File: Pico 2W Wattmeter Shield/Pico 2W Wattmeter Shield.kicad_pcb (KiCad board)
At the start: 2 copper layers, 53.3 x 22.9 mm, 23 parts, among them J1 RF In, U1 ADL5904, U2 ADS1115IDGS

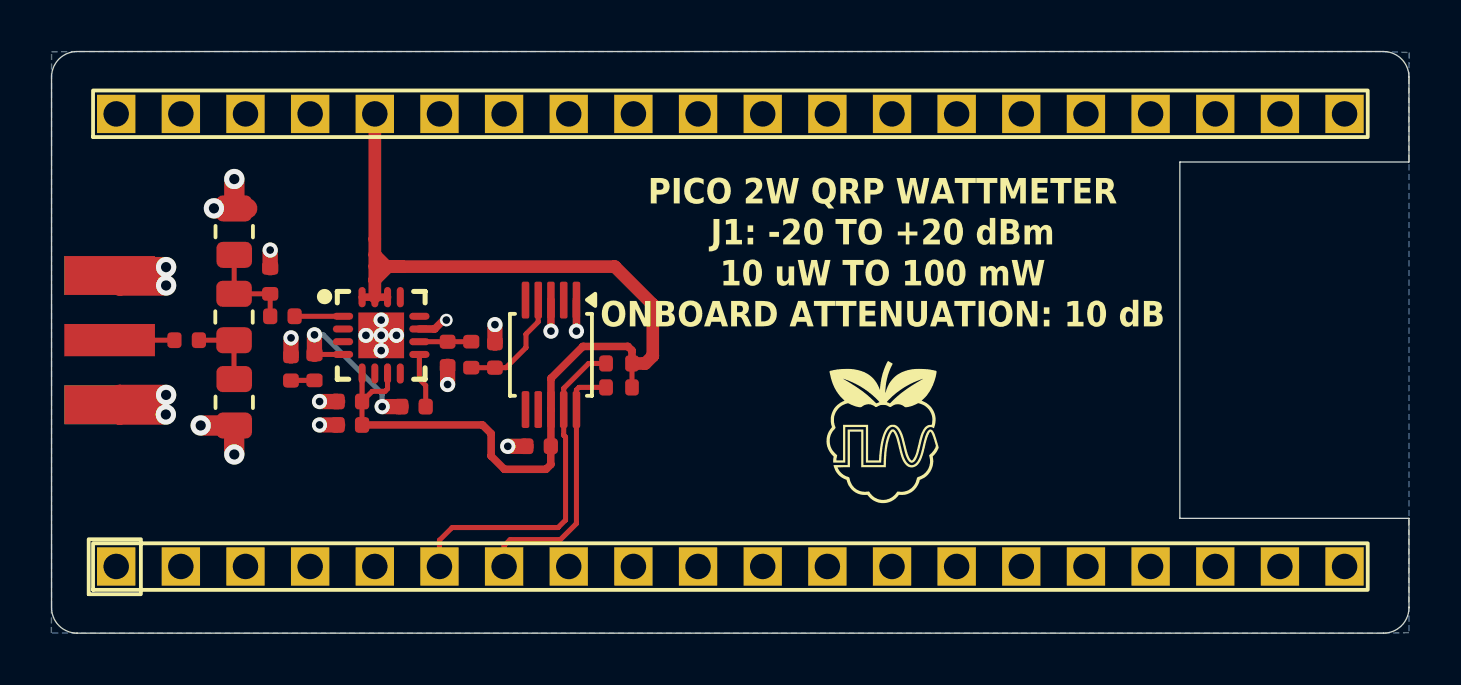
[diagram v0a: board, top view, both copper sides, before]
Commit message: Flip Pico shield assemblies and center USB reference markings
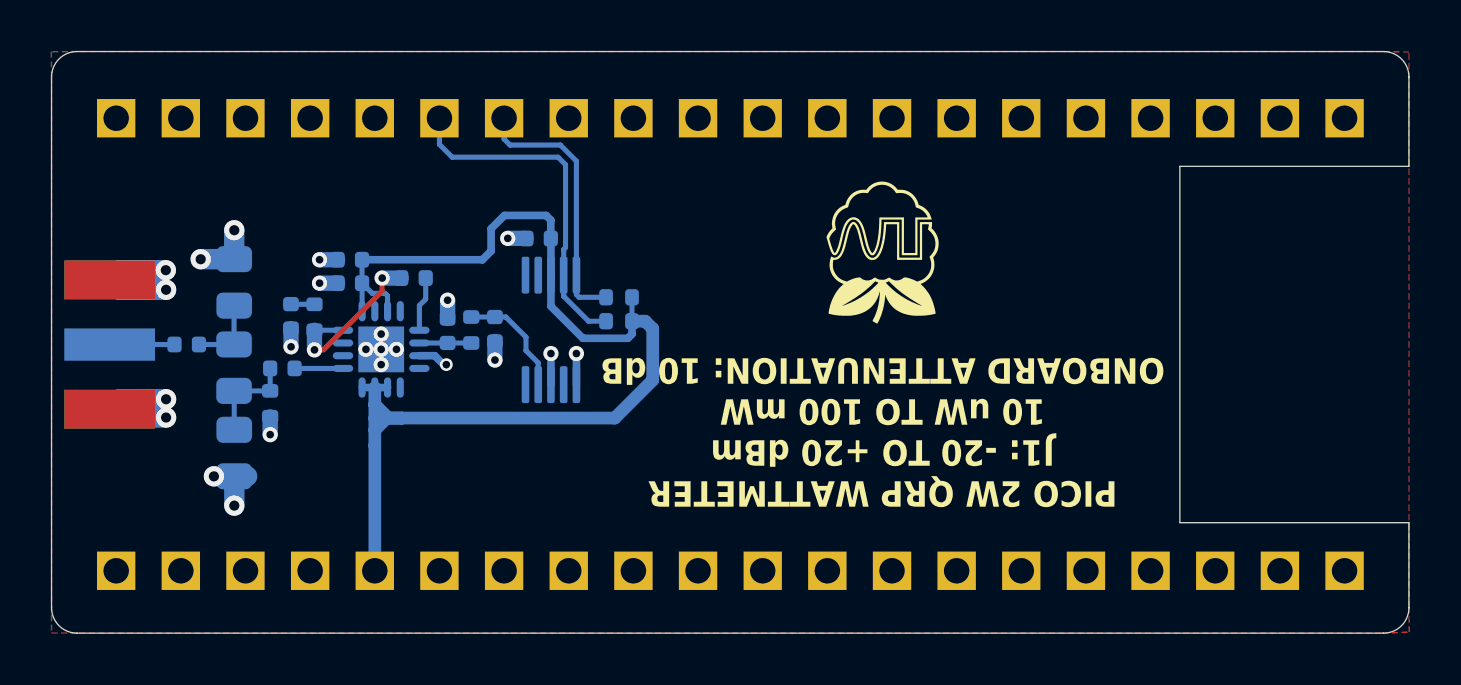
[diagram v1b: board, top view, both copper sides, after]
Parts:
- C1, C2, C3, C4, C5, C6, C7, C8, C9, J1, LOGO1, R1, R2, R3, R4, R5, R6, R7, R8, U1, U2, U3: moved to B.Cu
- LOGO2: moved to F.Cu
- moved R3 8.70 mm to (127.3, 94.1), turned to -90 degrees
- moved C9 8.16 mm to (139.3, 85.7)
- moved LOGO1 7.05 mm to (152.8, 86.2)
- moved LOGO2 7.05 mm to (152.8, 86.2)
- moved C5 6.49 mm to (131.8, 86.5)
- moved C6 5.05 mm to (134.3, 87.2)
- moved R4 4.83 mm to (128.7, 92.2), turned to -90 degrees
- moved R1 4.71 mm to (127.3, 87.4), turned to 90 degrees
- moved C4 4.65 mm to (131.8, 87.5)
- moved R7 3.54 mm to (142.4, 88.0)
- moved C2 2.05 mm to (129.2, 90.8)
- moved C3 2.04 mm to (129.5, 88.8), turned to -90 degrees
- moved R2 1.99 mm to (127.3, 90.8), turned to -90 degrees
- moved R5 1.97 mm to (130.5, 88.8), turned to 90 degrees
- moved U3 1.95 mm to (146.8, 90.8), turned to -90 degrees
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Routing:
- added copper zone on F.Cu, net GND
- removed copper zone on B.Cu, net GND
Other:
- outline, holes or cut-outs redrawn

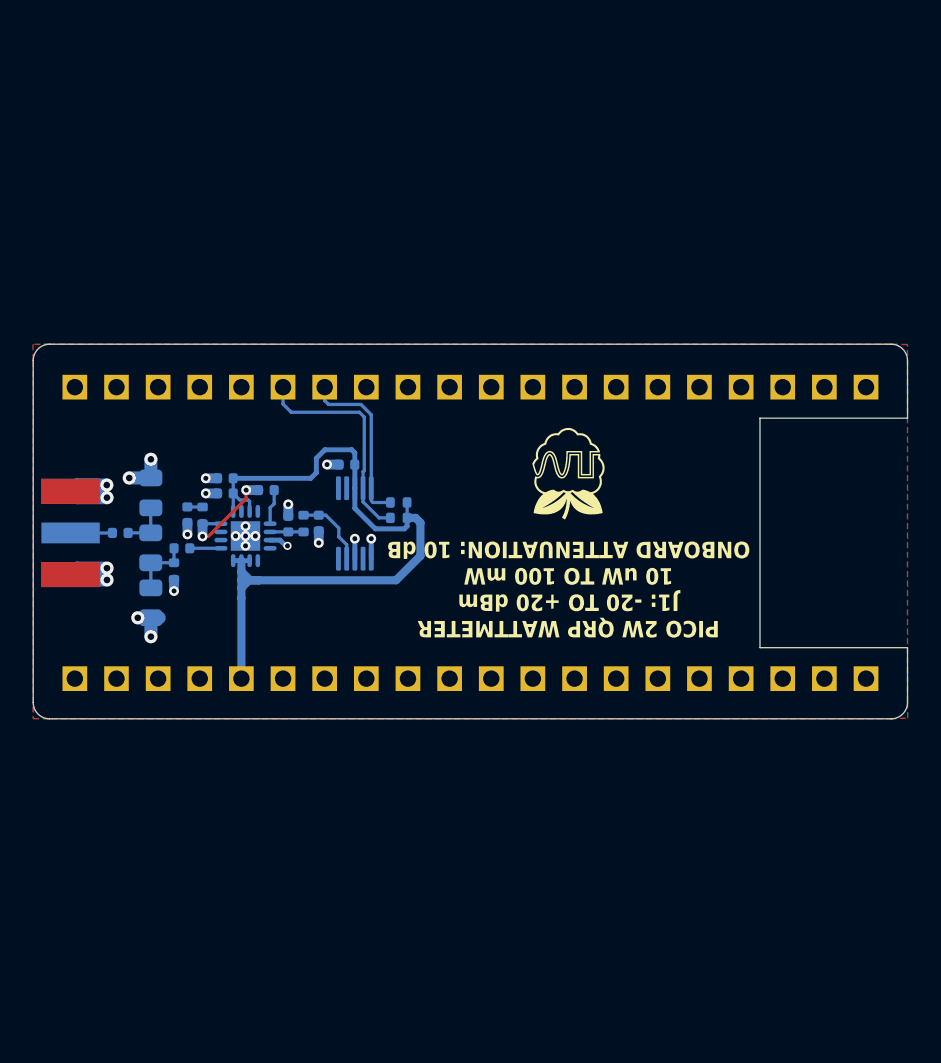
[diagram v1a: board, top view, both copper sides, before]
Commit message: Updated wattmeter design
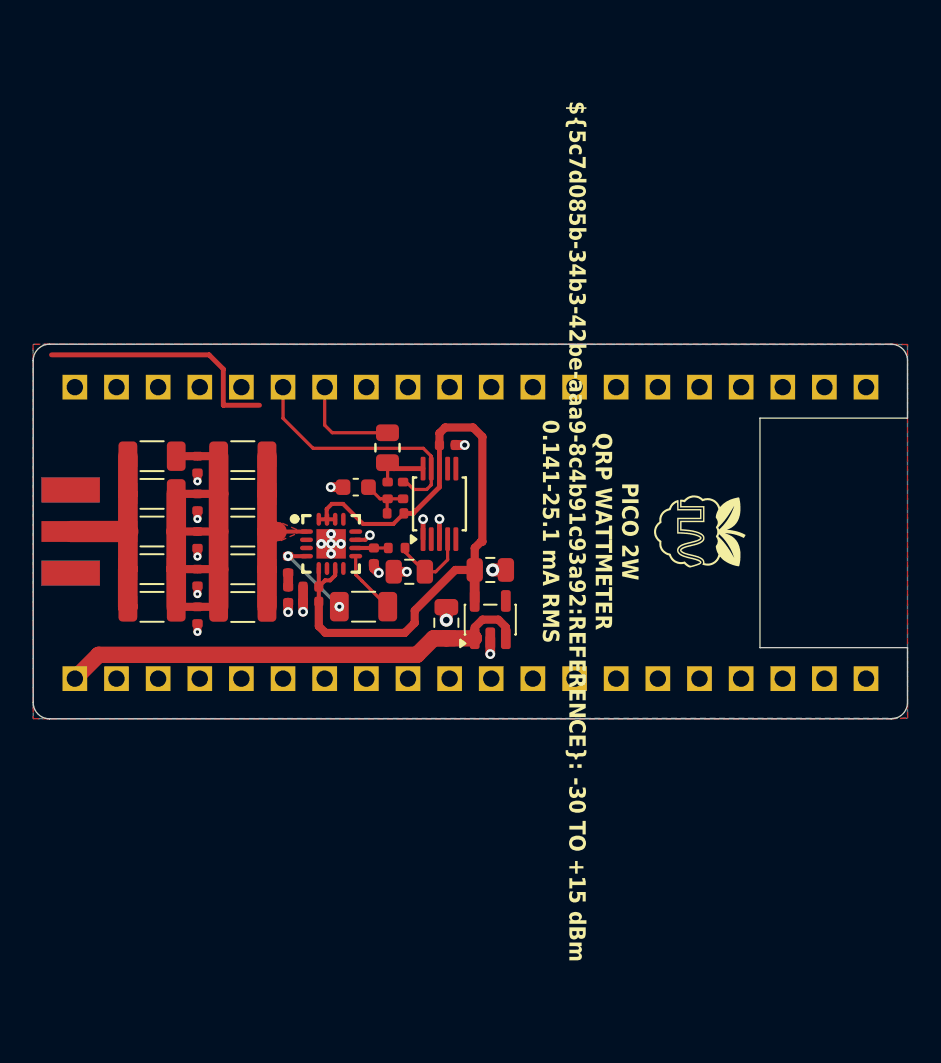
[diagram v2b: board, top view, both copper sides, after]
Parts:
- removed C1, C2: 470nF, pico-wattmeter:C_0402_1005Metric
- removed C3, C5, C6, C9: 100nF, pico-wattmeter:C_0402_1005Metric
- removed C4: 100pF, pico-wattmeter:C_0402_1005Metric
- removed C7: 10nF, pico-wattmeter:C_0402_1005Metric
- removed C8: 220nF, pico-wattmeter:C_0402_1005Metric
- removed J1: RF In, pico-wattmeter:SMA_Adafruit_1865_EdgeMount
- removed LOGO1: Wsprry_Pi_Synth_Logo, pico-wattmeter:Wsprry_Pi_Synth_Logo
- removed R1, R3: 97.6Ω, pico-wattmeter:R_0805_2012Metric
- removed R2: 71.5, pico-wattmeter:R_0805_2012Metric
- removed R4: 82.5Ω, pico-wattmeter:R_0402_1005Metric
- removed R5: 4.02Ω, pico-wattmeter:R_0402_1005Metric
- removed R6: 470Ω, pico-wattmeter:R_0402_1005Metric
- removed R7, R8: 4.7kΩ, pico-wattmeter:R_0402_1005Metric
- removed U1: ADL5904, pico-wattmeter:QFN-16_L3.0-W3.0-P0.50-TL-EP1.8
- removed U2: ADS1115IDGS, pico-wattmeter:TSSOP-10_3x3mm_P0.5mm
- removed U3: ~, pico-wattmeter:Raspberry_Pi_Pico_2W_Header
- added C20: 2.2μF, pico-wattmeter:C_0805_2012Metric, F.Cu at (145.3, 95.3)
- added C21: 2.2μF, pico-wattmeter:C_0805_2012Metric, F.Cu at (148.0, 92.1)
- added C30: 100nF, pico-wattmeter:C_1206_3216Metric, F.Cu at (127.4, 85.2)
- added C31: 100nF, pico-wattmeter:C_1206_3216Metric, F.Cu at (127.4, 87.5)
- added C32: 100nF, pico-wattmeter:C_1206_3216Metric, F.Cu at (127.4, 89.8)
- added C33: 100nF, pico-wattmeter:C_1206_3216Metric, F.Cu at (127.4, 92.1)
- added C34: 100nF, pico-wattmeter:C_1206_3216Metric, F.Cu at (127.4, 94.4)
- added C40: 100nF, pico-wattmeter:C_1206_3216Metric, F.Cu at (132.9, 85.2)
- added C41: 100nF, pico-wattmeter:C_1206_3216Metric, F.Cu at (132.9, 87.5)
- added C42: 100nF, pico-wattmeter:C_1206_3216Metric, F.Cu at (132.9, 89.8)
- added C43: 100nF, pico-wattmeter:C_1206_3216Metric, F.Cu at (132.9, 92.1)
- added C44: 100nF, pico-wattmeter:C_1206_3216Metric, F.Cu at (132.9, 94.4)
- added C45: 100nF, pico-wattmeter:C_0402_1005Metric, F.Cu at (135.7, 93.6)
- added C46: 100pF, pico-wattmeter:C_0402_1005Metric, F.Cu at (137.1, 93.1)
- added C47: 100nF, pico-wattmeter:C_0402_1005Metric, F.Cu at (137.1, 94.1)
- added C48: 100nF, pico-wattmeter:C_1206_3216Metric, F.Cu at (140.3, 94.4)
- added C49: 10nF, pico-wattmeter:C_0402_1005Metric, F.Cu at (140.9, 91.3)
- added C50: 22µF, pico-wattmeter:C_0805_2012Metric, F.Cu at (143.1, 92.2)
- added C60: 100nF, pico-wattmeter:C_0402_1005Metric, F.Cu at (145.4, 84.5)
- added C61: 1μF, pico-wattmeter:C_0603_1608Metric, F.Cu at (139.8, 87.1)
- added J30: RF In, pico-wattmeter:SMA_Adafruit_1865_EdgeMount, F.Cu at (120.1, 89.8)
- added R30: 412Ω, pico-wattmeter:R_0402_1005Metric, F.Cu at (130.2, 85.7)
- added R31: 412Ω, pico-wattmeter:R_0402_1005Metric, F.Cu at (130.2, 88.0)
- added R32: 412Ω, pico-wattmeter:R_0402_1005Metric, F.Cu at (130.2, 90.3)
- added R33: 412Ω, pico-wattmeter:R_0402_1005Metric, F.Cu at (130.2, 92.6)
- added R34: 412Ω, pico-wattmeter:R_0402_1005Metric, F.Cu at (130.2, 94.9)
- added R40: 4.02Ω, pico-wattmeter:R_0402_1005Metric, F.Cu at (135.7, 91.8)
- added R50: 470Ω, pico-wattmeter:R_0402_1005Metric, F.Cu at (142.3, 90.8)
- added R60: 4.7kΩ, pico-wattmeter:R_0402_1005Metric, F.Cu at (141.8, 87.3)
- added R61: 4.7kΩ, pico-wattmeter:R_0402_1005Metric, F.Cu at (142.7, 87.3)
- added R62: 0Ω, pico-wattmeter:R_0805_2012Metric, F.Cu at (141.7, 84.7)
- added R63: 47Ω, pico-wattmeter:R_0402_1005Metric, F.Cu at (142.2, 88.7)
- added U10: ~, pico-wattmeter:Raspberry_Pi_Pico_2W_Header, B.Cu at (146.8, 90.8)
- added U20: TPS7A2033, pico-wattmeter:SOT-23-5, F.Cu at (148.0, 95.1)
- added U40: ADL5904, pico-wattmeter:QFN-16_L3.0-W3.0-P0.50-TL-EP1.8, F.Cu at (138.3, 90.5)
- added U60: ADS1115IDGSR, pico-wattmeter:TSSOP-10_3x3mm_P0.5mm, F.Cu at (144.9, 88.1)
- moved LOGO2 8.75 mm to (160.8, 89.8), turned to -90 degrees
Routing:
- net +3V3: track 46.0 -> 0.00 mm
- net /ANALOG_3V3: track 0.00 -> 43.8 mm
- net /RF_DET_IN: track 0.00 -> 29.0 mm
- net /VBUS: track 0.00 -> 29.0 mm
- net /SDA: track 0.00 -> 15.7 mm
- net Net-(U2-SDA): track 13.6 -> 0.00 mm
- net Net-(J30-In): track 0.00 -> 12.7 mm
- net /RFIN: track 0.00 -> 11.6 mm
- net Net-(U2-SCL): track 10.5 -> 0.00 mm
- net Net-(U1-DECL): track 6.77 -> 0.00 mm, vias 2 -> 0
- net /SCL: track 0.00 -> 6.34 mm
- net GND: track 23.1 -> 28.7 mm, vias 23 -> 22
- net Net-(U40-DECL): track 0.00 -> 5.52 mm, vias 0 -> 2
- net /VRMS_FILTERED: track 0.00 -> 4.90 mm
- net Net-(U2-AIN0): track 4.54 -> 0.00 mm
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- added copper zone on F.Cu, net /RFIN
- added copper zone on B.Cu, net GND
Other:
- board text added: "FABRICATION REMINDER - SEVEN FILLED/CAPPED THROUGH VIAS Epoxy-fill, planarize, and copper-cap ONLY the five GND vias in ${5d9a238b-5df3-49c9-8cd2-6779ec770f50:REFERENCE} exposed pad 17 and the two DECL vias centered on ${4c44b8c8-c02e-4312-bb71-18f32a7e0676:REFERENCE} pad 1 and ${f595eb02-e28f-4346-a653-39831e8d909c:REFERENCE} pad 1. All seven: 0.60 mm copper / 0.25 mm drill, F.Cu-B.Cu. Keep F-si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"
- board text added: "PICO 2W QRP WATTMETER ${5c7d085b-34b3-42be-aaa9-8c4b91c93a92:REFERENCE}: -30 TO +15 dBm 0.141-25.1 mA RMS"
- board text removed: "FABRICATION REMINDER - U1 VIA-IN-PAD Order epoxy-filled, planarized, copper-capped vias (IPC-4761 Type VII). Apply ONLY to the five 0.30 mm vias inside U1 exposed pad 17. Other vias: retain their specified treatment. Identify the five vias in the fabrication drawing and order notes. Confirm selective treatment with the fabricator before production. This reminder alone does not enable via filling/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"
- board text removed: "PICO 2W QRP WATTMETER J1: -20 TO +20 dBm 10 uW TO 100 mW ONBOARD ATTENUATION: 10 dB"
